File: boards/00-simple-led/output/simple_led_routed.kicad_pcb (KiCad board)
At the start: 2 copper layers, 25 x 20 mm, 3 parts, among them J1 PWR

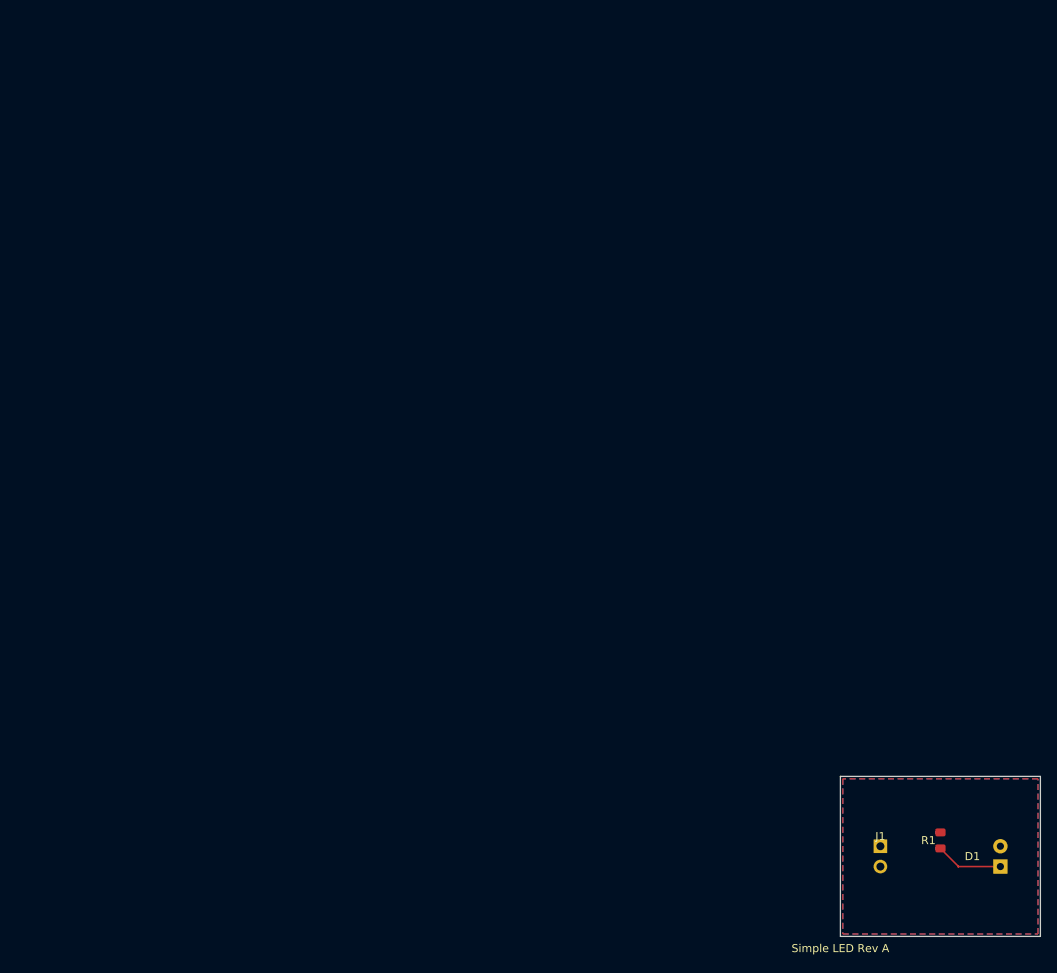
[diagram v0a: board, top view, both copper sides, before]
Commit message: feat(pcb): add page_fit to size sheet to board + center, apply to all boards
Add PCB.page_fit(margin=5.0) which rewrites the (paper ...) node to a tight
(paper "User" W H) sized to the Edge.Cuts bbox plus a uniform margin and
translates every board item (footprints, segments, vias, zones incl.
filled_polygons, gr_* graphics, text) so the board is centered with that
margin. Pure geometric translate — relative geometry, routing and DRC
validity are preserved, no re-route needed.

Expose it as `kct pcb page-fit <pcb> [-o out] [--margin] [--dry-run]` and
wire a PAGE_FIT build step (after stitch, before verify/export) so future
boards are centered too. Apply page_fit to all demo boards (00-07 +
external/softstart), both routed and unrouted PCBs, so the committed
layouts fill + center the KiCanvas viewer instead of sitting tiny in an A4
page. Boards 00/01 stay DRC-clean (0 errors); no board's DRC count changed.

Co-Authored-By: Claude Opus 4.7 <noreply@anthropic.com>
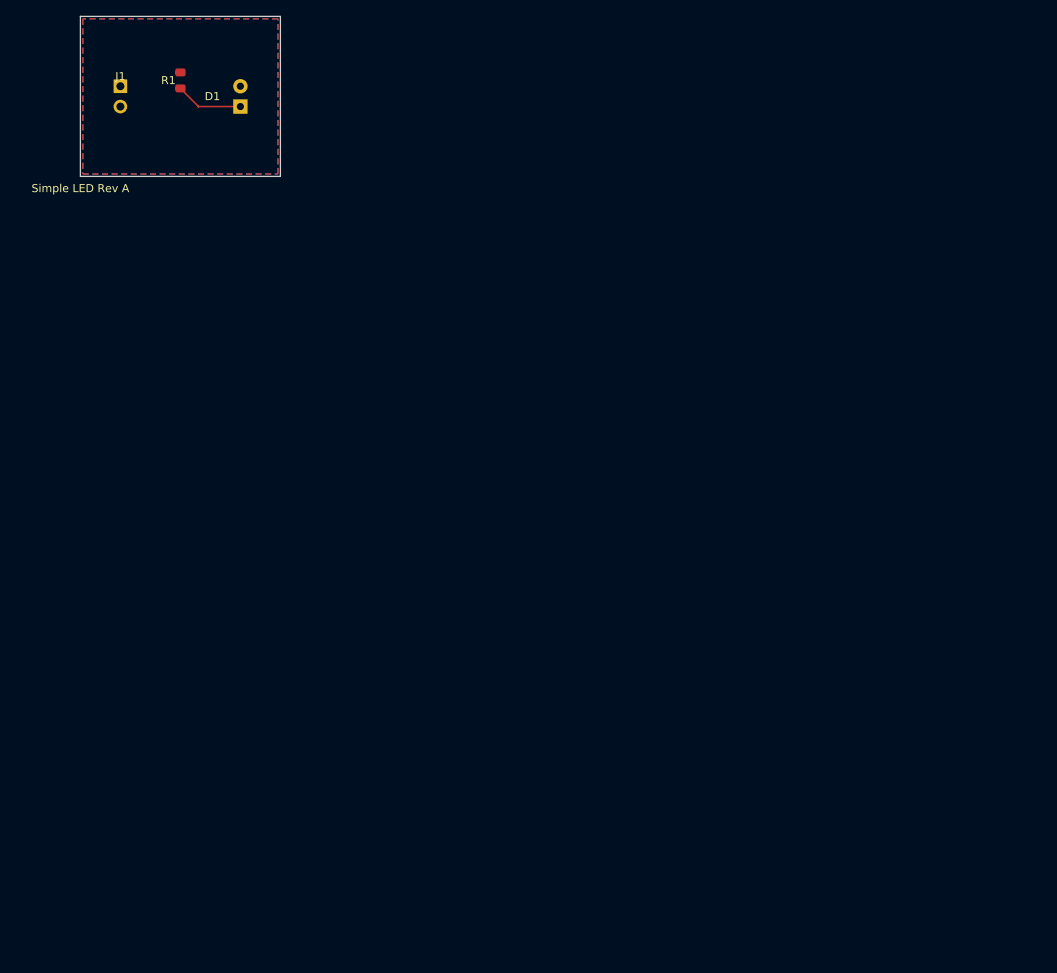
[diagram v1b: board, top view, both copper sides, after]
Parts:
- moved D1 134.4 mm to (25.0, 15.0)
- moved J1 134.4 mm to (10.0, 15.0)
- moved R1 134.4 mm to (17.5, 13.0)
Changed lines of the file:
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@@
 (kicad_pcb
 	(version 20260206)
+	(paper "User" 35 30)
 	(generator "pcbnew")
 	(generator_version "10.0")
@@
 		(legacy_teardrops no)
 	)
-	(paper "A4")
 	(layers
 		(0 "F.Cu" signal)
@@
 	(footprint "Connector_PinHeader_2.54mm:PinHeader_1x02_P2.54mm_Vertical"
 		(layer "F.Cu")
-		(at 105 110)
+		(at 10 15)
 		(property "Reference" "J1"
 			(at 0 -2.5 0)
@@
 	(footprint "LED_THT:LED_D5.0mm"
 		(layer "F.Cu")
-		(at 120 110 90)
+		(at 25 15 90)
 		(property "Reference" "D1"
 			(at 0 -3.5 0)
@@
 	(footprint "Resistor_SMD:R_0805_2012Metric"
 		(layer "F.Cu")
-		(at 112.5 108 90)
+		(at 17.5 13 90)
 		(property "Reference" "R1"
 			(at 0 -1.5 0)
@@
 	)
 	(gr_rect
-		(start 100 100)
-		(end 125 120)
+		(start 5 5)
+		(end 30 25)
 		(stroke
 			(width 0.1)
@@
 	)
 	(gr_text "Simple LED Rev A"
-		(at 100 121.5 0)
+		(at 5 26.5 0)
 		(layer "F.SilkS")
 		(effects
@@
 	)
 	(segment
-		(start 114.732 111.232)
-		(end 114.732 111.303)
+		(start 19.732 16.232)
+		(end 19.732 16.303)
 		(width 0.2)
 		(layer "F.Cu")
@@
 	)
 	(segment
-		(start 112.5 109)
-		(end 114.732 111.232)
+		(start 17.5 14)
+		(end 19.732 16.232)
 		(width 0.2)
 		(layer "F.Cu")
@@
 	)
 	(segment
-		(start 114.732 111.303)
-		(end 114.765 111.27)
+		(start 19.732 16.303)
+		(end 19.765 16.27)
 		(width 0.2)
 		(layer "F.Cu")
@@
 	)
 	(segment
-		(start 114.765 111.27)
-		(end 120 111.27)
+		(start 19.765 16.27)
+		(end 25 16.27)
 		(width 0.2)
 		(layer "F.Cu")
@@
 		(fill yes (thermal_gap 0.3) (thermal_bridge_width 0.4) (island_removal_mode 0)
 		)
-		(polygon (pts (xy 100.3 100.3) (xy 100.3 119.7) (xy 124.7 119.7) (xy 124.7 100.3))
+		(polygon (pts (xy 5.3 5.3) (xy 5.3 24.7) (xy 29.7 24.7) (xy 29.7 5.3))
 		)
 	)
@@
 		(fill yes (thermal_gap 0.3) (thermal_bridge_width 0.4) (island_removal_mode 0)
 		)
-		(polygon (pts (xy 100.3 100.3) (xy 100.3 119.7) (xy 124.7 119.7) (xy 124.7 100.3))
-		)
-	)
+		(polygon (pts (xy 5.3 5.3) (xy 5.3 24.7) (xy 29.7 24.7) (xy 29.7 5.3))
+		)
+	)

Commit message: fix(board-00): rotation-0 footprints + deterministic LED_ANODE route → 0 DRC under both engines
Board 00 (simple-led) shipped genuine copper shorts under kicad-cli
(GND↔LED_ANODE, LED_ANODE↔VCC, plus the matching front solder-mask
bridges). Root cause: R1 and D1 were placed at a 90° rotation, and
kicad-tools' internal pad-position transform (kct check, the autorouter,
zone fill) models KiCad's on-disk footprint angle as a counter-clockwise
math rotation, whereas KiCad applies it clockwise in its Y-down frame.
For cardinal 90°/270° rotations the two conventions place pin 1 vs pin 2
at mirror-image positions, so the autorouter wired LED_ANODE to R1's VCC
pad and D1's GND pad (a real short kicad-cli flagged) while kct check —
using the same mirrored convention as the router — saw it as "correct".
No single routing could satisfy both engines.

Fix (board-local, no shared-code change):
- Place every footprint at rotation 0, where sin(angle)=0 and both
  conventions agree on pad positions. Board 00 was the only demo board
  using a 90° rotation, so this removes the ambiguity without affecting
  any other board (all others already use 0°).
- Replace the grid autorouter's LED_ANODE result (which still grazed D1's
  GND pad) with a deterministic L-shaped route derived from the actual
  pad positions, clearing the foreign GND pad with margin.

Result: kicad-cli DRC 0 shorts / 0 solder_mask_bridge / 0 unconnected /
0 isolated_copper; kct check --mfr jlcpcb --errors-only = 0; CI strict
routed-DRC gate = 0; report.md DRC Status = PASS. Manufacturing bundle
regenerated with --mfr jlcpcb-tier1.

Closes #3737

Co-Authored-By: Claude Opus 4.7 <noreply@anthropic.com>
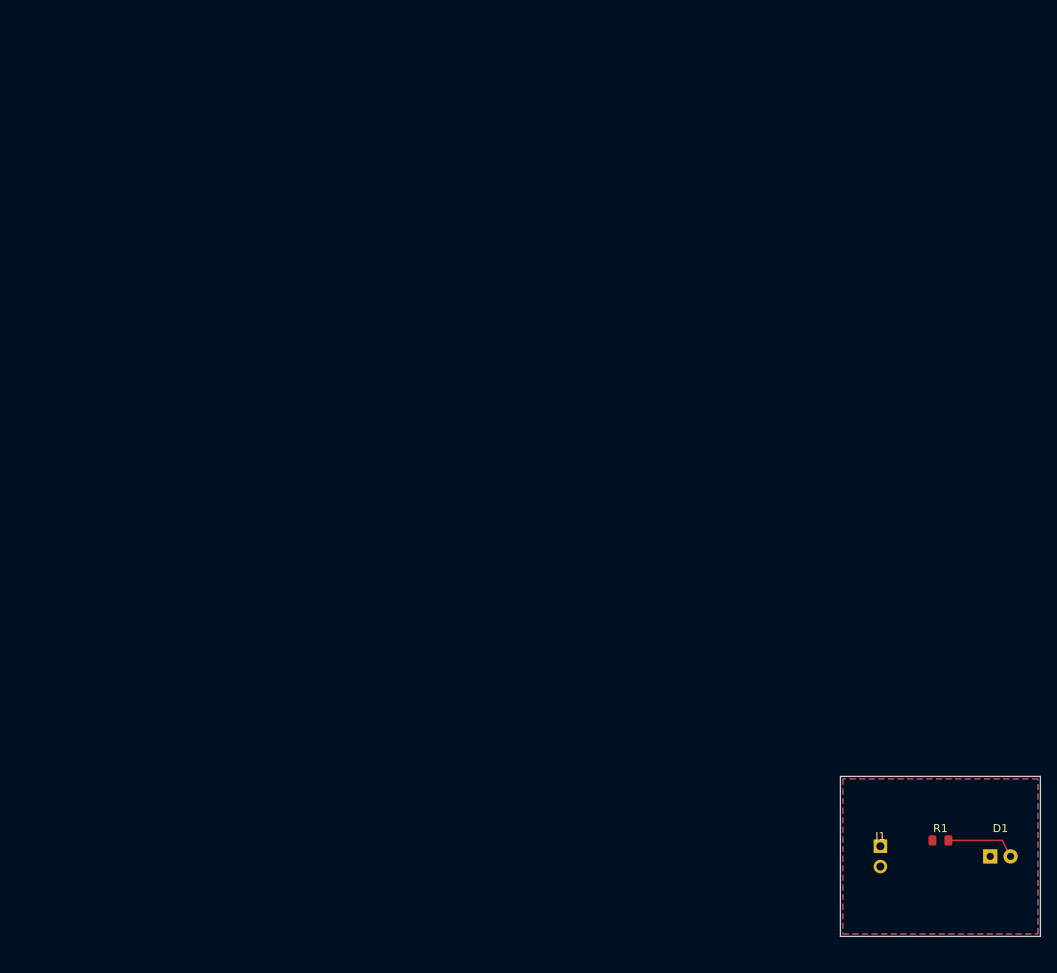
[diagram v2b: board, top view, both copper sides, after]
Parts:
- moved D1 134.4 mm to (120.0, 110.0), turned to 0 degrees
- moved J1 134.4 mm to (105.0, 110.0)
- moved R1 134.4 mm to (112.5, 108.0), turned to 0 degrees
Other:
- board text removed: "Simple LED Rev A"
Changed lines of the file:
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@@
 (kicad_pcb
 	(version 20260206)
-	(paper "User" 35 30)
 	(generator "pcbnew")
 	(generator_version "10.0")
@@
 		(legacy_teardrops no)
 	)
+	(paper "A4")
 	(layers
 		(0 "F.Cu" signal)
@@
 	(net 2 "LED_ANODE")
 	(net 3 "GND")
+	(footprint "Resistor_SMD:R_0805_2012Metric"
+		(layer "F.Cu")
+		(at 112.5 108)
+		(property "Reference" "R1"
+			(at 0 -1.5 0)
+			(layer "F.SilkS")
+			(effects
+				(font
+					(size 1 1)
+					(thickness 0.15)
+				)
+			)
+		)
+		(property "Value" "330"
+			(at 0 1.5 0)
+			(layer "F.Fab")
+			(effects
+				(font
+					(size 1 1)
+					(thickness 0.15)
+				)
+			)
+		)
+		(property "Datasheet" ""
+			(at 0 0 0)
+			(layer "F.Fab")
+			(hide yes)
+			(effects
+				(font
+					(size 1.27 1.27)
+				)
+			)
+		)
+		(property "Description" ""
+			(at 0 0 0)
+			(layer "F.Fab")
+			(hide yes)
+			(effects
+				(font
+					(size 1.27 1.27)
+				)
+			)
+		)
+		(duplicate_pad_numbers_are_jumpers no)
+		(pad "1" smd roundrect
+			(at -1 0)
+			(size 1 1.3)
+			(layers "F.Cu" "F.Mask" "F.Paste")
+			(roundrect_rratio 0.25)
+			(zone_connect 2)
+			(net 1 "VCC")
+		)
+		(pad "2" smd roundrect
+			(at 1 0)
+			(size 1 1.3)
+			(layers "F.Cu" "F.Mask" "F.Paste")
+			(roundrect_rratio 0.25)
+			(net 2 "LED_ANODE")
+		)
+		(embedded_fonts no)
+	)
 	(footprint "Connector_PinHeader_2.54mm:PinHeader_1x02_P2.54mm_Vertical"
 		(layer "F.Cu")
-		(at 10 15)
+		(at 105 110)
 		(property "Reference" "J1"
 			(at 0 -2.5 0)
@@
 	(footprint "LED_THT:LED_D5.0mm"
 		(layer "F.Cu")
-		(at 25 15 90)
+		(at 120 110)
 		(property "Reference" "D1"
 			(at 0 -3.5 0)
@@
 		)
 		(property "Datasheet" ""
-			(at 0 0 90)
+			(at 0 0 0)
 			(layer "F.Fab")
 			(hide yes)
@@
 		)
 		(property "Description" ""
-			(at 0 0 90)
+			(at 0 0 0)
 			(layer "F.Fab")
 			(hide yes)
@@
 		(duplicate_pad_numbers_are_jumpers no)
 		(pad "1" thru_hole rect
-			(at -1.27 0 90)
+			(at -1.27 0)
 			(size 1.8 1.8)
 			(drill 0.9)
@@
 		)
 		(pad "2" thru_hole circle
-			(at 1.27 0 90)
+			(at 1.27 0)
 			(size 1.8 1.8)
 			(drill 0.9)
@@
 		(embedded_fonts no)
 	)
-	(footprint "Resistor_SMD:R_0805_2012Metric"
-		(layer "F.Cu")
-		(at 17.5 13 90)
-		(property "Reference" "R1"
-			(at 0 -1.5 0)
-			(layer "F.SilkS")
-			(effects
-				(font
-					(size 1 1)
-					(thickness 0.15)
-				)
-			)
-		)
-		(property "Value" "330"
-			(at 0 1.5 0)
-			(layer "F.Fab")
-			(effects
-				(font
-					(size 1 1)
-					(thickness 0.15)
-				)
-			)
-		)
-		(property "Datasheet" ""
-			(at 0 0 90)
-			(layer "F.Fab")
-			(hide yes)
-			(effects
-				(font
-					(size 1.27 1.27)
-				)
-			)
-		)
-		(property "Description" ""
-			(at 0 0 90)
-			(layer "F.Fab")
-			(hide yes)
-			(effects
-				(font
-					(size 1.27 1.27)
-				)
-			)
-		)
-		(duplicate_pad_numbers_are_jumpers no)
-		(pad "1" smd roundrect
-			(at -1 0 90)
-			(size 1 1.3)
-			(layers "F.Cu" "F.Mask" "F.Paste")
-			(roundrect_rratio 0.25)
-			(net 1 "VCC")
-		)
-		(pad "2" smd roundrect
-			(at 1 0 90)
-			(size 1 1.3)
-			(layers "F.Cu" "F.Mask" "F.Paste")
-			(roundrect_rratio 0.25)
-			(net 2 "LED_ANODE")
-		)
-		(embedded_fonts no)
-	)
 	(gr_rect
-		(start 5 5)
-		(end 30 25)
+		(start 100 100)
+		(end 125 120)
 		(stroke
 			(width 0.1)
@@
 		(layer "Edge.Cuts")
 	)
-	(gr_text "Simple LED Rev A"
-		(at 5 26.5 0)
-		(layer "F.SilkS")
-		(effects
-			(font
-				(size 1 1)
-				(thickness 0.15)
-			)
-		)
-	)
 	(segment
-		(start 19.732 16.232)
-		(end 19.732 16.303)
+		(start 120.23 108)
+		(end 121.27 110)
 		(width 0.2)
 		(layer "F.Cu")
@@
 	)
 	(segment
-		(start 17.5 14)
-		(end 19.732 16.232)
-		(width 0.2)
-		(layer "F.Cu")
-		(net 2)
-	)
-	(segment
-		(start 19.732 16.303)
-		(end 19.765 16.27)
-		(width 0.2)
-		(layer "F.Cu")
-		(net 2)
-	)
-	(segment
-		(start 19.765 16.27)
-		(end 25 16.27)
+		(start 113.5 108)
+		(end 120.23 108)
 		(width 0.2)
 		(layer "F.Cu")
@@
 		(fill yes (thermal_gap 0.3) (thermal_bridge_width 0.4) (island_removal_mode 0)
 		)
-		(polygon (pts (xy 5.3 5.3) (xy 5.3 24.7) (xy 29.7 24.7) (xy 29.7 5.3))
+		(polygon (pts (xy 100.3 100.3) (xy 100.3 119.7) (xy 124.7 119.7) (xy 124.7 100.3))
 		)
 	)
@@
 		(fill yes (thermal_gap 0.3) (thermal_bridge_width 0.4) (island_removal_mode 0)
 		)
-		(polygon (pts (xy 5.3 5.3) (xy 5.3 24.7) (xy 29.7 24.7) (xy 29.7 5.3))
-		)
-	)
+		(polygon (pts (xy 100.3 100.3) (xy 100.3 119.7) (xy 124.7 119.7) (xy 124.7 100.3))
+		)
+	)
